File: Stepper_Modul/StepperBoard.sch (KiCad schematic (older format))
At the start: 11 parts, among them J101 Screw_Terminal_01x02, J102 Screw_Terminal_01x04, J103 Screw_Terminal_01x04, J104 Screw_Terminal_01x04, J105 Screw_Terminal_01x04, J106 Conn_02x20_Odd_Even

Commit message: stepper board fertig gestellt
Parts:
- removed F101: Fuse, Fuse:Fuseholder_Cylinder-5x20mm_Schurter_0031_8201_Horizontal_Open, symbol Device:Fuse
- added Q101: Si4431CDY, Package_SO:SOIC-8_3.9x4.9mm_P1.27mm, symbol PorjectLibrary:Si4431CDY
- added R101, R102: 22K1, Resistor_SMD:R_0603_1608Metric, symbol Device:R_Small
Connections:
- net +24V: now also Q101.5 (S), Q101.6 (S), Q101.7 (S), Q101.8 (S), R101.2
- net CUR_ROT: now also J106.5 (Pin_5); no longer J106.1 (Pin_1)
- net CUR_X: now also J106.21 (Pin_21); no longer J106.18 (Pin_18)
- net CUR_Y: now also J106.27 (Pin_27); no longer J106.17 (Pin_17)
- net CUR_Z: now also J106.11 (Pin_11); no longer J106.2 (Pin_2)
- net DIAG_ROT: now also J106.2 (Pin_2); no longer J106.7 (Pin_7)
- net DIAG_X: now also J106.18 (Pin_18); no longer J106.24 (Pin_24)
- net DIAG_Y: now also J106.24 (Pin_24); no longer J106.23 (Pin_23)
- net DIR_ROT: now also J106.6 (Pin_6); no longer J106.5 (Pin_5)
- net DIR_Y: now also J106.28 (Pin_28); no longer J106.21 (Pin_21)
- net DIR_Z: now also J106.12 (Pin_12); no longer J106.6 (Pin_6)
- net EN_ROT: now also J106.1 (Pin_1); no longer J106.11 (Pin_11)
- net EN_X: now also J106.17 (Pin_17); no longer J106.28 (Pin_28)
- net EN_Y: now also J106.23 (Pin_23); no longer J106.27 (Pin_27)
- net EN_Z: now also J106.7 (Pin_7); no longer J106.12 (Pin_12)
- net GND: now also J101.2 (Pin_2), R102.1; no longer J101.1 (Pin_1)
- net INDEX_ROT: now also J106.3 (Pin_3); no longer J106.9 (Pin_9)
- net INDEX_X: now also J106.19 (Pin_19); no longer J106.26 (Pin_26)
- net INDEX_Z: now also J106.9 (Pin_9); no longer J106.10 (Pin_10)
- net STEP_ROT: now also J106.4 (Pin_4); no longer J106.3 (Pin_3)
- net STEP_Y: now also J106.26 (Pin_26); no longer J106.19 (Pin_19)
- net STEP_Z: now also J106.10 (Pin_10); no longer J106.4 (Pin_4)
- new net: J101.1 (Pin_1), Q101.1 (D), Q101.2 (D), Q101.3 (D)
- new net: Q101.4 (G), R101.1, R102.2
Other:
- note added: "Same resistor as in CPU-Board\nto reduce BOM\n"
- moved on the sheet: J101
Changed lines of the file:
@@
 L Connector:Screw_Terminal_01x02 J101
 U 1 1 5FBE8C83
-P 3200 1500
-F 0 "J101" H 3120 1085 50  0000 C CNN
-F 1 "Screw_Terminal_01x02" H 3120 1176 50  0000 C CNN
-F 2 "TerminalBlock_RND:TerminalBlock_RND_205-00045_1x02_P5.00mm_Horizontal" H 3200 1500 50  0001 C CNN
-F 3 "https://datasheet.lcsc.com/szlcsc/1912251636_Ningbo-Kangnex-Elec-WJ301V-5-0-2P_C8475.pdf" H 3200 1500 50  0001 C CNN
-F 4 "C8475" H 3120 1267 50  0000 C CNN "LCSC"
-	1    3200 1500
-	-1   0    0    1
+P 1500 1400
+F 0 "J101" H 1420 985 50  0000 C CNN
+F 1 "Screw_Terminal_01x02" H 1420 1076 50  0000 C CNN
+F 2 "TerminalBlock_RND:TerminalBlock_RND_205-00045_1x02_P5.00mm_Horizontal" H 1500 1400 50  0001 C CNN
+F 3 "https://datasheet.lcsc.com/szlcsc/1912251636_Ningbo-Kangnex-Elec-WJ301V-5-0-2P_C8475.pdf" H 1500 1400 50  0001 C CNN
+F 4 "C8475" H 1420 1167 50  0000 C CNN "LCSC"
+	1    1500 1400
+	-1   0    0    -1
 $EndComp
 $Comp
 L power:+24V #PWR0112
 U 1 1 5FC10E36
-P 4850 1400
-F 0 "#PWR0112" H 4850 1250 50  0001 C CNN
-F 1 "+24V" H 4865 1573 50  0000 C CNN
-F 2 "" H 4850 1400 50  0001 C CNN
-F 3 "" H 4850 1400 50  0001 C CNN
-	1    4850 1400
+P 3700 1400
+F 0 "#PWR0112" H 3700 1250 50  0001 C CNN
+F 1 "+24V" H 3715 1573 50  0000 C CNN
+F 2 "" H 3700 1400 50  0001 C CNN
+F 3 "" H 3700 1400 50  0001 C CNN
+	1    3700 1400
 	1    0    0    -1
 $EndComp
@@
 L power:GND #PWR0113
 U 1 1 5FC11289
-P 4850 1500
-F 0 "#PWR0113" H 4850 1250 50  0001 C CNN
-F 1 "GND" H 4855 1327 50  0000 C CNN
-F 2 "" H 4850 1500 50  0001 C CNN
-F 3 "" H 4850 1500 50  0001 C CNN
-	1    4850 1500
+P 2600 2200
+F 0 "#PWR0113" H 2600 1950 50  0001 C CNN
+F 1 "GND" H 2605 2027 50  0000 C CNN
+F 2 "" H 2600 2200 50  0001 C CNN
+F 3 "" H 2600 2200 50  0001 C CNN
+	1    2600 2200
 	1    0    0    -1
 $EndComp
@@
 F12 "OB2_ROT" O R 9050 1350 50
 $EndSheet
-Wire Wire Line
-	4250 1400 4450 1400
-Wire Wire Line
-	3400 1500 4450 1500
 $Comp
 L power:+3V3 #PWR?
@@
 Wire Wire Line
 	7300 1800 7850 1800
+Text Label 3150 2850 0    50   ~ 0
+CUR_ROT
+Text Label 4750 2750 2    50   ~ 0
+STEP_ROT
+Text Label 4750 2850 2    50   ~ 0
+DIR_ROT
+Text Label 4750 2650 2    50   ~ 0
+DIAG_ROT
+Text Label 3150 2750 0    50   ~ 0
+INDEX_ROT
 Text Label 3150 2650 0    50   ~ 0
-CUR_ROT
-Text Label 3150 2750 0    50   ~ 0
-STEP_ROT
-Text Label 3150 2850 0    50   ~ 0
-DIR_ROT
-Text Label 3150 2950 0    50   ~ 0
-DIAG_ROT
-Text Label 3150 3050 0    50   ~ 0
-INDEX_ROT
-Text Label 3150 3150 0    50   ~ 0
 EN_ROT
 Wire Wire Line
 	3150 2650 3700 2650
 Wire Wire Line
+	4750 2650 4200 2650
+Wire Wire Line
 	3150 2750 3700 2750
 Wire Wire Line
+	4750 2750 4200 2750
+Wire Wire Line
 	3150 2850 3700 2850
 Wire Wire Line
-	3150 2950 3700 2950
-Wire Wire Line
-	3150 3050 3700 3050
-Wire Wire Line
-	3150 3150 3700 3150
+	4750 2850 4200 2850
 Text Label 7300 2600 0    50   ~ 0
 CUR_Z
@@
 Wire Wire Line
 	7300 3200 7850 3200
-Text Label 4750 2650 2    50   ~ 0
+Text Label 3150 3150 0    50   ~ 0
 CUR_Z
-Text Label 4750 2750 2    50   ~ 0
+Text Label 4750 3050 2    50   ~ 0
 STEP_Z
-Text Label 4750 2850 2    50   ~ 0
+Text Label 4750 3150 2    50   ~ 0
 DIR_Z
 Text Label 4750 2950 2    50   ~ 0
 DIAG_Z
-Text Label 4750 3050 2    50   ~ 0
+Text Label 3150 3050 0    50   ~ 0
 INDEX_Z
-Text Label 4750 3150 2    50   ~ 0
+Text Label 3150 2950 0    50   ~ 0
 EN_Z
 Wire Wire Line
-	4750 2650 4200 2650
-Wire Wire Line
-	4750 2750 4200 2750
-Wire Wire Line
-	4750 2850 4200 2850
+	3150 2950 3700 2950
 Wire Wire Line
 	4750 2950 4200 2950
 Wire Wire Line
+	3150 3050 3700 3050
+Wire Wire Line
 	4750 3050 4200 3050
+Wire Wire Line
+	3150 3150 3700 3150
 Wire Wire Line
 	4750 3150 4200 3150
@@
 Wire Wire Line
 	7300 4650 7850 4650
-Text Label 3150 3450 0    50   ~ 0
+Text Label 3150 3950 0    50   ~ 0
 CUR_Y
-Text Label 3150 3550 0    50   ~ 0
+Text Label 4750 3850 2    50   ~ 0
 STEP_Y
-Text Label 3150 3650 0    50   ~ 0
+Text Label 4750 3950 2    50   ~ 0
 DIR_Y
-Text Label 3150 3750 0    50   ~ 0
+Text Label 4750 3750 2    50   ~ 0
 DIAG_Y
 Text Label 3150 3850 0    50   ~ 0
 INDEX_Y
-Text Label 3150 3950 0    50   ~ 0
+Text Label 3150 3750 0    50   ~ 0
 EN_Y
 Wire Wire Line
-	3150 3450 3700 3450
-Wire Wire Line
-	3150 3550 3700 3550
-Wire Wire Line
-	3150 3650 3700 3650
-Wire Wire Line
 	3150 3750 3700 3750
 Wire Wire Line
+	4750 3750 4200 3750
+Wire Wire Line
 	3150 3850 3700 3850
 Wire Wire Line
+	4750 3850 4200 3850
+Wire Wire Line
 	3150 3950 3700 3950
-Text Label 4750 3450 2    50   ~ 0
+Wire Wire Line
+	4750 3950 4200 3950
+Text Label 3150 3650 0    50   ~ 0
 CUR_X
 Text Label 4750 3550 2    50   ~ 0
@@
 Text Label 4750 3650 2    50   ~ 0
 DIR_X
-Text Label 4750 3750 2    50   ~ 0
+Text Label 4750 3450 2    50   ~ 0
 DIAG_X
-Text Label 4750 3850 2    50   ~ 0
+Text Label 3150 3550 0    50   ~ 0
 INDEX_X
 Text Label 4750 4150 2    50   ~ 0
 SINGLE_WIRE
-Text Label 4750 3950 2    50   ~ 0
+Text Label 3150 3450 0    50   ~ 0
 EN_X
 Wire Wire Line
+	3150 3450 3700 3450
+Wire Wire Line
 	4750 3450 4200 3450
 Wire Wire Line
+	3150 3550 3700 3550
+Wire Wire Line
 	4750 3550 4200 3550
 Wire Wire Line
+	3150 3650 3700 3650
+Wire Wire Line
+	4200 4150 4750 4150
+Wire Wire Line
 	4750 3650 4200 3650
-Wire Wire Line
-	4750 3750 4200 3750
-Wire Wire Line
-	4750 3850 4200 3850
-Wire Wire Line
-	4200 4150 4750 4150
-Wire Wire Line
-	4750 3950 4200 3950
 $Comp
 L power:GND #PWR0147
@@
 Wire Wire Line
 	3700 4450 2550 4450
-$Comp
-L Device:Fuse F101
-U 1 1 600F6E53
-P 4100 1400
-F 0 "F101" V 3903 1400 50  0000 C CNN
-F 1 "Fuse" V 3994 1400 50  0000 C CNN
-F 2 "Fuse:Fuseholder_Cylinder-5x20mm_Schurter_0031_8201_Horizontal_Open" V 4030 1400 50  0001 C CNN
-F 3 "~" H 4100 1400 50  0001 C CNN
-F 4 "C58066" V 4100 1400 50  0001 C CNN "LCSC"
-	1    4100 1400
-	0    1    1    0
-$EndComp
-Wire Wire Line
-	3950 1400 3400 1400
 $Comp
 L power:GND #PWR0150
@@
 L power:PWR_FLAG #FLG0106
 U 1 1 601606ED
-P 4450 1150
-F 0 "#FLG0106" H 4450 1225 50  0001 C CNN
-F 1 "PWR_FLAG" H 4450 1324 50  0000 C CNN
-F 2 "" H 4450 1150 50  0001 C CNN
-F 3 "~" H 4450 1150 50  0001 C CNN
-	1    4450 1150
-	1    0    0    -1
-$EndComp
-Wire Wire Line
-	4450 1150 4450 1400
-Connection ~ 4450 1400
-Wire Wire Line
-	4450 1400 4850 1400
+P 3300 1150
+F 0 "#FLG0106" H 3300 1225 50  0001 C CNN
+F 1 "PWR_FLAG" H 3300 1324 50  0000 C CNN
+F 2 "" H 3300 1150 50  0001 C CNN
+F 3 "~" H 3300 1150 50  0001 C CNN
+	1    3300 1150
+	1    0    0    -1
+$EndComp
+Wire Wire Line
+	3300 1150 3300 1400
+Connection ~ 3300 1400
+Wire Wire Line
+	3300 1400 3700 1400
 $Comp
 L power:PWR_FLAG #FLG0107
 U 1 1 60164631
-P 4450 1750
-F 0 "#FLG0107" H 4450 1825 50  0001 C CNN
-F 1 "PWR_FLAG" H 4450 1923 50  0000 C CNN
-F 2 "" H 4450 1750 50  0001 C CNN
-F 3 "~" H 4450 1750 50  0001 C CNN
-	1    4450 1750
+P 2200 2450
+F 0 "#FLG0107" H 2200 2525 50  0001 C CNN
+F 1 "PWR_FLAG" H 2200 2623 50  0000 C CNN
+F 2 "" H 2200 2450 50  0001 C CNN
+F 3 "~" H 2200 2450 50  0001 C CNN
+	1    2200 2450
 	-1   0    0    1
 $EndComp
 Wire Wire Line
-	4450 1750 4450 1500
-Connection ~ 4450 1500
-Wire Wire Line
-	4450 1500 4850 1500
+	2200 2450 2200 2200
+Connection ~ 2200 2200
+Wire Wire Line
+	2200 2200 2600 2200
 $Comp
 L Mechanical:MountingHole_Pad H101
@@
 Wire Wire Line
 	3350 6800 3350 6600
+Wire Wire Line
+	2600 1500 2600 1400
+Wire Wire Line
+	2600 1400 2550 1400
+Connection ~ 2600 1400
+Wire Wire Line
+	2350 1800 2350 1700
+Wire Wire Line
+	2600 1700 2600 1800
+Connection ~ 2600 1800
+Wire Wire Line
+	2600 1800 2350 1800
+Wire Wire Line
+	2600 1900 2600 1800
+$Comp
+L PorjectLibrary:Si4431CDY Q101
+U 1 1 600D5FDB
+P 2350 1500
+F 0 "Q101" V 2784 1500 50  0000 C CNN
+F 1 "Si4431CDY" V 2693 1500 50  0000 C CNN
+F 2 "Package_SO:SOIC-8_3.9x4.9mm_P1.27mm" H 2550 1600 50  0001 C CNN
+F 3 "https://datasheet.lcsc.com/szlcsc/Vishay-Intertech-SI4431CDY-T1-GE3_C144845.pdf" H 2350 1500 50  0001 C CNN
+F 4 "C144845" V 2602 1500 50  0000 C CNN "LCSC"
+	1    2350 1500
+	0    1    -1   0
+$EndComp
+Wire Wire Line
+	1700 1500 1700 2200
+Wire Wire Line
+	1700 2200 2200 2200
+Wire Wire Line
+	1700 1400 2150 1400
+Wire Wire Line
+	2600 1400 3300 1400
+$Comp
+L Device:R_Small R101
+U 1 1 6010C1B8
+P 2600 1600
+AR Path="/6010C1B8" Ref="R101"  Part="1"
+AR Path="/5ED2496F/6010C1B8" Ref="R?"  Part="1"
+AR Path="/5FDD0F66/6010C1B8" Ref="R?"  Part="1"
+F 0 "R101" H 2450 1600 50  0000 C CNN
+F 1 "22K1" H 2400 1700 50  0000 C CNN
+F 2 "Resistor_SMD:R_0603_1608Metric" H 2600 1600 50  0001 C CNN
+F 3 "~" H 2600 1600 50  0001 C CNN
+F 4 "C137768" H 2600 1600 50  0001 C CNN "LCSC"
+	1    2600 1600
+	-1   0    0    1
+$EndComp
+$Comp
+L Device:R_Small R102
+U 1 1 601157F0
+P 2600 2000
+AR Path="/601157F0" Ref="R102"  Part="1"
+AR Path="/5ED2496F/601157F0" Ref="R?"  Part="1"
+AR Path="/5FDD0F66/601157F0" Ref="R?"  Part="1"
+F 0 "R102" H 2450 2000 50  0000 C CNN
+F 1 "22K1" H 2400 2100 50  0000 C CNN
+F 2 "Resistor_SMD:R_0603_1608Metric" H 2600 2000 50  0001 C CNN
+F 3 "~" H 2600 2000 50  0001 C CNN
+F 4 "C137768" H 2600 2000 50  0001 C CNN "LCSC"
+	1    2600 2000
+	-1   0    0    1
+$EndComp
+Wire Wire Line
+	2600 2100 2600 2200
+Connection ~ 2600 2200
+Text Notes 2950 1900 0    50   ~ 0
+Same resistor as in CPU-Board\nto reduce BOM\n
 $EndSCHEMATC

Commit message: Feeder Microswitch für Tape Motor hinzugefügt. Einige 3D Step Modelle hinzugefügt. Stepper Board die Ecken abgerundet.
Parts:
- J101: footprint TerminalBlock_RND:TerminalBlock_RND_205-00045_1x02_P5.00mm_Horizontal -> ProjectFootprints:TerminalBlock_RND_205-00045_1x02_P5.00mm_Horizontal
- J102, J103, J104, J105: footprint TerminalBlock_RND:TerminalBlock_RND_205-00047_1x04_P5.00mm_Horizontal -> ProjectFootprints:TerminalBlock_RND_205-00047_1x04_P5.00mm_Horizontal
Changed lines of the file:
@@
 EESchema Schematic File Version 4
-LIBS:StepperBoard-cache
-EELAYER 26 0
+EELAYER 30 0
 EELAYER END
 $Descr A4 11693 8268
@@
 F 0 "J105" H 9780 5637 50  0000 L CNN
 F 1 "Screw_Terminal_01x04" H 9780 5546 50  0000 L CNN
-F 2 "TerminalBlock_RND:TerminalBlock_RND_205-00047_1x04_P5.00mm_Horizontal" H 9700 5600 50  0001 C CNN
+F 2 "ProjectFootprints:TerminalBlock_RND_205-00047_1x04_P5.00mm_Horizontal" H 9700 5600 50  0001 C CNN
 F 3 "https://datasheet.lcsc.com/szlcsc/1912251636_Ningbo-Kangnex-Elec-WJ301V-5-0-2P_C8475.pdf" H 9700 5600 50  0001 C CNN
 F 4 "C8475" H 9780 5455 50  0000 L CNN "LCSC"
@@
 F 0 "J104" H 9780 4337 50  0000 L CNN
 F 1 "Screw_Terminal_01x04" H 9780 4246 50  0000 L CNN
-F 2 "TerminalBlock_RND:TerminalBlock_RND_205-00047_1x04_P5.00mm_Horizontal" H 9700 4300 50  0001 C CNN
+F 2 "ProjectFootprints:TerminalBlock_RND_205-00047_1x04_P5.00mm_Horizontal" H 9700 4300 50  0001 C CNN
 F 3 "https://datasheet.lcsc.com/szlcsc/1912251636_Ningbo-Kangnex-Elec-WJ301V-5-0-2P_C8475.pdf" H 9700 4300 50  0001 C CNN
 F 4 "C8475" H 9780 4155 50  0000 L CNN "LCSC"
@@
 F 0 "J103" H 9780 2887 50  0000 L CNN
 F 1 "Screw_Terminal_01x04" H 9780 2796 50  0000 L CNN
-F 2 "TerminalBlock_RND:TerminalBlock_RND_205-00047_1x04_P5.00mm_Horizontal" H 9700 2850 50  0001 C CNN
+F 2 "ProjectFootprints:TerminalBlock_RND_205-00047_1x04_P5.00mm_Horizontal" H 9700 2850 50  0001 C CNN
 F 3 "https://datasheet.lcsc.com/szlcsc/1912251636_Ningbo-Kangnex-Elec-WJ301V-5-0-2P_C8475.pdf" H 9700 2850 50  0001 C CNN
 F 4 "C8475" H 9780 2705 50  0000 L CNN "LCSC"
@@
 F 0 "J102" H 9780 1487 50  0000 L CNN
 F 1 "Screw_Terminal_01x04" H 9780 1396 50  0000 L CNN
-F 2 "TerminalBlock_RND:TerminalBlock_RND_205-00047_1x04_P5.00mm_Horizontal" H 9700 1450 50  0001 C CNN
+F 2 "ProjectFootprints:TerminalBlock_RND_205-00047_1x04_P5.00mm_Horizontal" H 9700 1450 50  0001 C CNN
 F 3 "https://datasheet.lcsc.com/szlcsc/1912251636_Ningbo-Kangnex-Elec-WJ301V-5-0-2P_C8475.pdf" H 9700 1450 50  0001 C CNN
 F 4 "C8475" H 9780 1305 50  0000 L CNN "LCSC"
@@
 F 0 "J101" H 1420 985 50  0000 C CNN
 F 1 "Screw_Terminal_01x02" H 1420 1076 50  0000 C CNN
-F 2 "TerminalBlock_RND:TerminalBlock_RND_205-00045_1x02_P5.00mm_Horizontal" H 1500 1400 50  0001 C CNN
+F 2 "ProjectFootprints:TerminalBlock_RND_205-00045_1x02_P5.00mm_Horizontal" H 1500 1400 50  0001 C CNN
 F 3 "https://datasheet.lcsc.com/szlcsc/1912251636_Ningbo-Kangnex-Elec-WJ301V-5-0-2P_C8475.pdf" H 1500 1400 50  0001 C CNN
 F 4 "C8475" H 1420 1167 50  0000 C CNN "LCSC"

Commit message: BOM für LCSC überarbeitet. Tool für BOM export modifiziert
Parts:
- H101, H102, H103, H104: LCSC (none) -> 0
- J106: LCSC (none) -> C601944
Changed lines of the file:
@@
 F 2 "Connector_PinHeader_2.54mm:PinHeader_2x20_P2.54mm_Vertical" H 3900 3550 50  0001 C CNN
 F 3 "~" H 3900 3550 50  0001 C CNN
+F 4 "C601944" H 3900 3550 50  0001 C CNN "LCSC"
 	1    3900 3550
 	1    0    0    -1
@@
 F 2 "MountingHole:MountingHole_3.2mm_M3_Pad_Via" H 3450 6200 50  0001 C CNN
 F 3 "~" H 3450 6200 50  0001 C CNN
+F 4 "0" H 3450 6200 50  0001 C CNN "LCSC"
 	1    3450 6200
 	0    1    1    0
@@
 F 2 "MountingHole:MountingHole_3.2mm_M3_Pad_Via" H 3450 6400 50  0001 C CNN
 F 3 "~" H 3450 6400 50  0001 C CNN
+F 4 "0" H 3450 6400 50  0001 C CNN "LCSC"
 	1    3450 6400
 	0    1    1    0
@@
 F 2 "MountingHole:MountingHole_3.2mm_M3_Pad_Via" H 3450 6600 50  0001 C CNN
 F 3 "~" H 3450 6600 50  0001 C CNN
+F 4 "0" H 3450 6600 50  0001 C CNN "LCSC"
 	1    3450 6600
 	0    1    1    0
@@
 F 2 "MountingHole:MountingHole_3.2mm_M3_Pad_Via" H 3450 6800 50  0001 C CNN
 F 3 "~" H 3450 6800 50  0001 C CNN
+F 4 "0" H 3450 6800 50  0001 C CNN "LCSC"
 	1    3450 6800
 	0    1    1    0

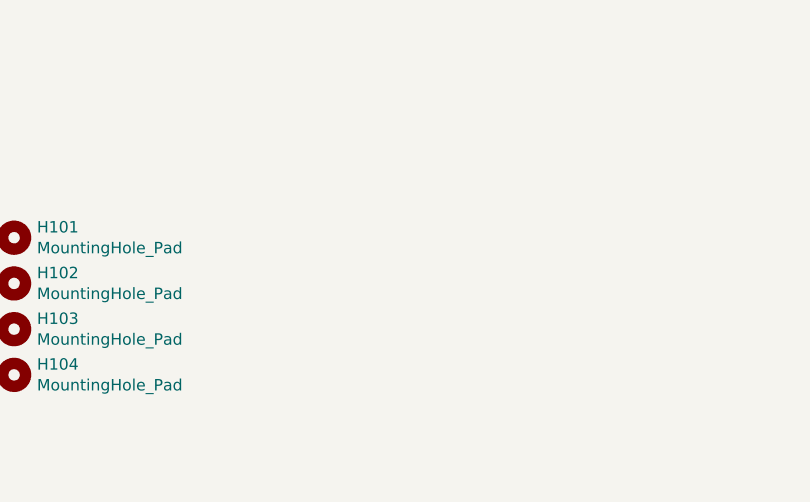
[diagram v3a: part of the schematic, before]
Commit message: Fiducials auf allen Boards hinzugefügt
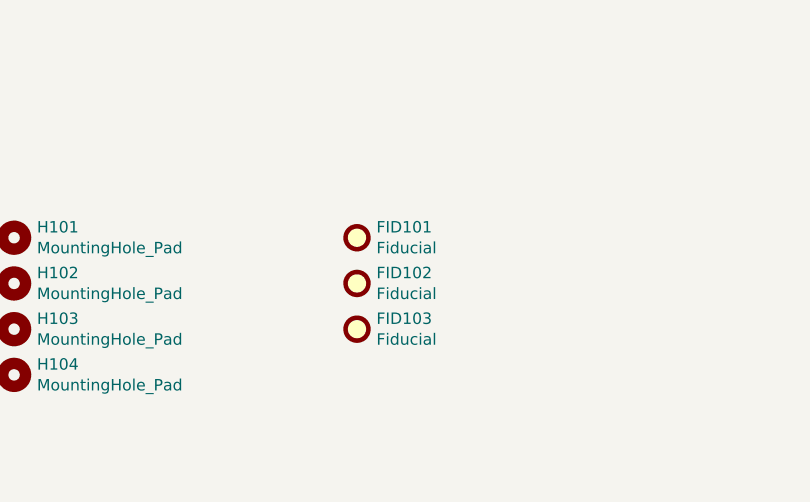
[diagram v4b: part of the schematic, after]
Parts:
- added FID101, FID102, FID103: Fiducial, Fiducial:Fiducial_1mm_Mask2mm, symbol Mechanical:Fiducial
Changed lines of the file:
@@
 Text Notes 2950 1900 0    50   ~ 0
 Same resistor as in CPU-Board\nto reduce BOM\n
+$Comp
+L Mechanical:Fiducial FID101
+U 1 1 602BDED6
+P 5000 6200
+F 0 "FID101" H 5085 6246 50  0000 L CNN
+F 1 "Fiducial" H 5085 6155 50  0000 L CNN
+F 2 "Fiducial:Fiducial_1mm_Mask2mm" H 5000 6200 50  0001 C CNN
+F 3 "~" H 5000 6200 50  0001 C CNN
+	1    5000 6200
+	1    0    0    -1
+$EndComp
+$Comp
+L Mechanical:Fiducial FID102
+U 1 1 602BE652
+P 5000 6400
+F 0 "FID102" H 5085 6446 50  0000 L CNN
+F 1 "Fiducial" H 5085 6355 50  0000 L CNN
+F 2 "Fiducial:Fiducial_1mm_Mask2mm" H 5000 6400 50  0001 C CNN
+F 3 "~" H 5000 6400 50  0001 C CNN
+	1    5000 6400
+	1    0    0    -1
+$EndComp
+$Comp
+L Mechanical:Fiducial FID103
+U 1 1 602BE98D
+P 5000 6600
+F 0 "FID103" H 5085 6646 50  0000 L CNN
+F 1 "Fiducial" H 5085 6555 50  0000 L CNN
+F 2 "Fiducial:Fiducial_1mm_Mask2mm" H 5000 6600 50  0001 C CNN
+F 3 "~" H 5000 6600 50  0001 C CNN
+	1    5000 6600
+	1    0    0    -1
+$EndComp
 $EndSCHEMATC

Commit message: Änderungen für bestellung V01 -  Bestellung abgeschickt
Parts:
- FID101, FID102, FID103: LCSC (none) -> 0
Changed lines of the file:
@@
 F 2 "Fiducial:Fiducial_1mm_Mask2mm" H 5000 6200 50  0001 C CNN
 F 3 "~" H 5000 6200 50  0001 C CNN
+F 4 "0" H 5000 6200 50  0001 C CNN "LCSC"
 	1    5000 6200
 	1    0    0    -1
@@
 F 2 "Fiducial:Fiducial_1mm_Mask2mm" H 5000 6400 50  0001 C CNN
 F 3 "~" H 5000 6400 50  0001 C CNN
+F 4 "0" H 5000 6400 50  0001 C CNN "LCSC"
 	1    5000 6400
 	1    0    0    -1
@@
 F 2 "Fiducial:Fiducial_1mm_Mask2mm" H 5000 6600 50  0001 C CNN
 F 3 "~" H 5000 6600 50  0001 C CNN
+F 4 "0" H 5000 6600 50  0001 C CNN "LCSC"
 	1    5000 6600
 	1    0    0    -1
